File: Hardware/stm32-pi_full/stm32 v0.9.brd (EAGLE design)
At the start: 131.4 x 105.8 mm, 272 parts, among them J1 SOLDERJUMPERNO, Q1 MMBT3906, Q2 MMBT3904, Q3 MMBT3904, U1 ESP32-WROOM-32D, Y1 6MM_3.5MM_CRYSTAL

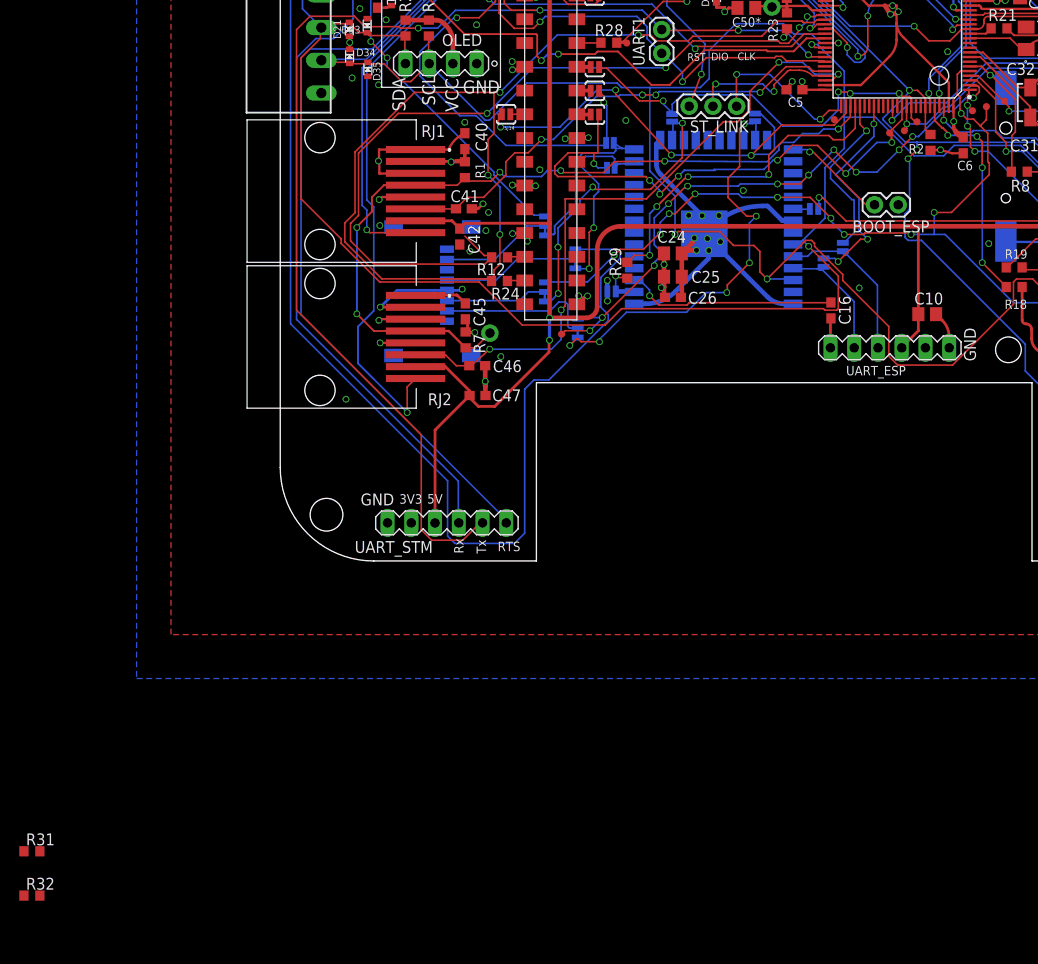
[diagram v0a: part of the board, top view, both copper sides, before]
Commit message: non-Blocking UART transmissions
Saving 40ms at 460800 baud or 160ms at 115200 baud.
Now takes less than a millisecond to begin the UART transmit, happens in the background.
notes included on how to fire UART transmissions consequtively withing messing up the buffer or dropping transmissions.
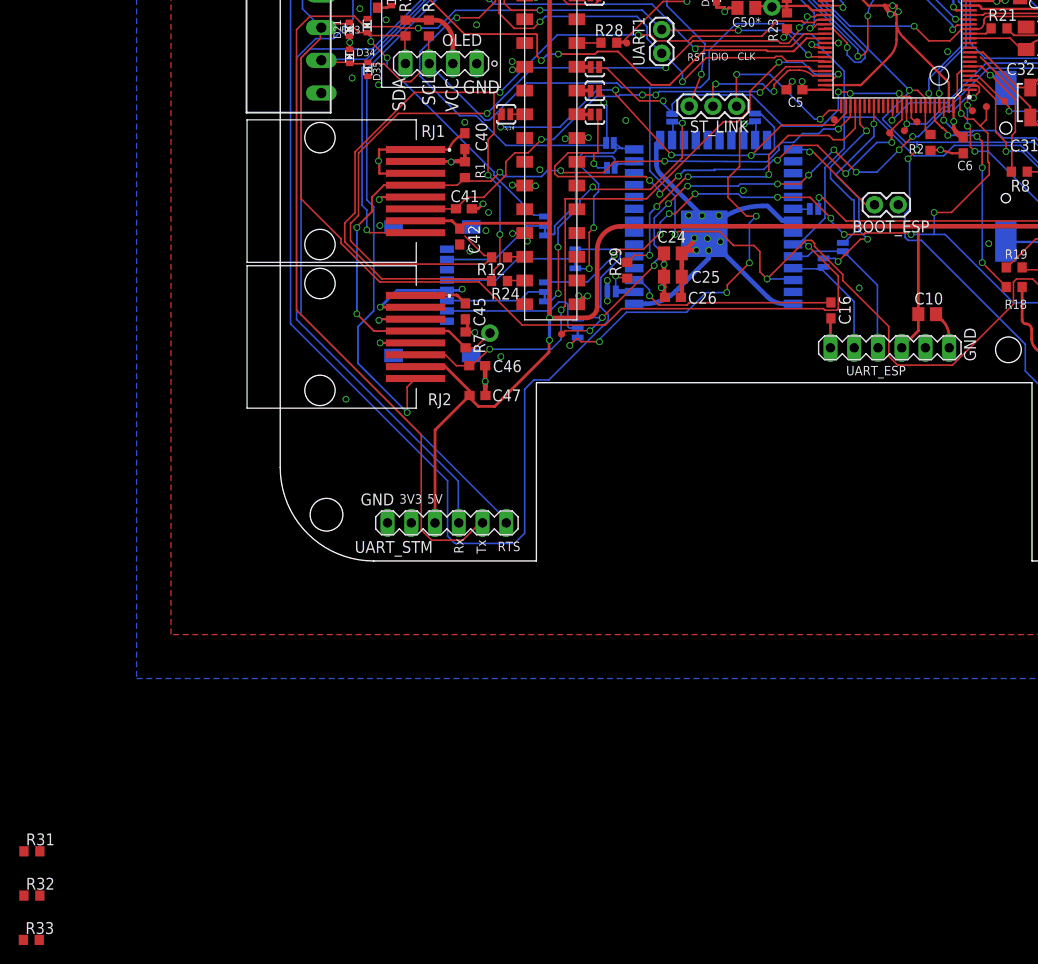
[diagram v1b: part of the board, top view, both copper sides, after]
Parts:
- added R33: 0R, rcl:R0603
- C29, C30: value 4.7nF -> 15pF
- C31, C32: value 2.2uF -> 10pF
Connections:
- new net N$1: R33.2, STM32F303VE.8
- net PC14: now also R33.1; no longer STM32F303VE.8
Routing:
- net PC14: track 12.9 -> 11.7 mm
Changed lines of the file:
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@@
 <attribute name="VALUE" x="120.97" y="40.14" size="1.27" layer="27" rot="R180"/>
 </element>
-<element name="C29" library="rcl" library_urn="urn:adsk.eagle:library:334" package="C0603" package3d_urn="urn:adsk.eagle:package:23616/2" value="4.7nF" x="87.0936875" y="57.0890375" smashed="yes">
+<element name="C29" library="rcl" library_urn="urn:adsk.eagle:library:334" package="C0603" package3d_urn="urn:adsk.eagle:package:23616/2" value="15pF" x="87.0936875" y="57.0890375" smashed="yes">
 <attribute name="NAME" x="88.71165625" y="58.977115625" size="1.27" layer="25" rot="R270"/>
 <attribute name="POPULARITY" value="73" x="87.0936875" y="57.0890375" size="1.778" layer="27" display="off"/>
@@
 <attribute name="VALUE" x="86.4586875" y="55.1840375" size="1.27" layer="27"/>
 </element>
-<element name="C30" library="rcl" library_urn="urn:adsk.eagle:library:334" package="C0603" package3d_urn="urn:adsk.eagle:package:23616/2" value="4.7nF" x="87.10355" y="54.8606875" smashed="yes">
+<element name="C30" library="rcl" library_urn="urn:adsk.eagle:library:334" package="C0603" package3d_urn="urn:adsk.eagle:package:23616/2" value="15pF" x="87.10355" y="54.8606875" smashed="yes">
 <attribute name="NAME" x="85.607396875" y="52.7083" size="1.27" layer="25"/>
 <attribute name="POPULARITY" value="73" x="87.10355" y="54.8606875" size="1.778" layer="27" display="off"/>
@@
 <attribute name="VALUE" x="86.46855" y="52.9556875" size="1.27" layer="27"/>
 </element>
-<element name="C31" library="rcl" library_urn="urn:adsk.eagle:library:334" package="C0805" package3d_urn="urn:adsk.eagle:package:23617/2" value="2.2uF" x="83.002" y="45.078" smashed="yes">
+<element name="C31" library="rcl" library_urn="urn:adsk.eagle:library:334" package="C0805" package3d_urn="urn:adsk.eagle:package:23617/2" value="10pF" x="83.002" y="45.078" smashed="yes">
 <attribute name="NAME" x="78.045440625" y="43.81645" size="1.27" layer="25"/>
 <attribute name="POPULARITY" value="88" x="83.002" y="45.078" size="1.778" layer="27" display="off"/>
@@
 <attribute name="VALUE" x="81.732" y="42.538" size="1.27" layer="27"/>
 </element>
-<element name="C32" library="rcl" library_urn="urn:adsk.eagle:library:334" package="C0805" package3d_urn="urn:adsk.eagle:package:23617/2" value="2.2uF" x="83" y="52.5" smashed="yes">
+<element name="C32" library="rcl" library_urn="urn:adsk.eagle:library:334" package="C0805" package3d_urn="urn:adsk.eagle:package:23617/2" value="10pF" x="83" y="52.5" smashed="yes">
 <attribute name="NAME" x="77.667828125" y="51.983675" size="1.27" layer="25"/>
 <attribute name="POPULARITY" value="88" x="83" y="52.5" size="1.778" layer="27" display="off"/>
@@
 <attribute name="VALUE" x="-27.197559375" y="-37.693090625" size="1.27" layer="27"/>
 </element>
+<element name="R33" library="rcl" library_urn="urn:adsk.eagle:library:334" package="R0603" package3d_urn="urn:adsk.eagle:package:23555/3" value="0R" x="-26.62351875" y="-40.529509375" smashed="yes">
+<attribute name="NAME" x="-27.25851875" y="-39.894509375" size="1.27" layer="25"/>
+<attribute name="POPULARITY" value="70" x="-26.62351875" y="-40.529509375" size="1.778" layer="27" display="off"/>
+<attribute name="SPICEPREFIX" value="R" x="-26.62351875" y="-40.529509375" size="1.778" layer="27" display="off"/>
+<attribute name="VALUE" x="-27.25851875" y="-42.434509375" size="1.27" layer="27"/>
+</element>
 </elements>
 <signals>
@@
 </signal>
 <signal name="PC14">
-<contactref element="STM32F303VE" pad="8"/>
 <contactref element="LSE" pad="P$1"/>
-<wire x1="73.75" y1="53.9" x2="74.9036375" y2="53.9" width="0.2032" layer="1"/>
 <wire x1="80.226" y1="48.5776375" x2="80.226" y2="47.438" width="0.2032" layer="1"/>
 <wire x1="74.9036375" y1="53.9" x2="80.226" y2="48.5776375" width="0.2032" layer="1"/>
@@
 <wire x1="80.226" y1="47.438" x2="81.67440625" y2="45.98959375" width="0.254" layer="1"/>
 <wire x1="81.67440625" y1="45.98959375" x2="82.052" y2="45.078" width="0.254" layer="1" curve="-45"/>
+<contactref element="R33" pad="1"/>
+<wire x1="-27.47351875" y1="-40.529509375" x2="82.052" y2="45.078" width="0" layer="19" extent="1-1"/>
 </signal>
 <signal name="PC15">
@@
 <via x="35.8775" y="30.48" extent="1-16" drill="0.5"/>
 </signal>
+<signal name="N$1">
+<contactref element="STM32F303VE" pad="8"/>
+<contactref element="R33" pad="2"/>
+<wire x1="-25.77351875" y1="-40.529509375" x2="73.75" y2="53.9" width="0" layer="19" extent="1-1"/>
+</signal>
 </signals>

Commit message: minor, uipdate BoMs
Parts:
- R21: value 0R -> 2k
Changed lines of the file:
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@@
 <attribute name="VALUE" x="11.495" y="57.635" size="1.27" layer="27" rot="R270"/>
 </element>
-<element name="R21" library="resistor" package="R0603" value="0R" x="76.883209375" y="56.964225" smashed="yes">
+<element name="R21" library="resistor" package="R0603" value="2k" x="76.883209375" y="56.964225" smashed="yes">
 <attribute name="NAME" x="78.810725" y="59.036134375" size="1.27" layer="25" rot="R180"/>
 <attribute name="VALUE" x="76.248209375" y="55.059225" size="1.27" layer="27"/>

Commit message: minor changes, some checks on proto v0.8 done.
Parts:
- removed Q4: (no value), microbuilder:SOT23-R
- added C20, C34: 100nF, rcl:C0603
- added D36, D37: ESD5Z3.3T1G, microbuilder:SOD-523
- R34, R35, R36: value (none) -> 0R
- R8: value 1.5k -> 100k
- renumbered JP4 to R34, JP5 to R35, JP6 to R36
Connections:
- new net N$19: D37.K, R8.1
- net +3V3: no longer Q4.3
- net +5V: now also D36.A
- net GND: now also C20.2; no longer Q4.1
- net N$16: now also D36.K, D37.A; no longer Q4.2, R8.1
- net NRST_STM: now also C34.1, C34.2
- net VBAT: now also C20.1
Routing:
- net N$16: track 1.93 -> 0.00 mm
- net BIAS: track 588.4 -> 587.1 mm
- net GND: track 296.9 -> 295.6 mm, vias 143 -> 142
- net +3V3: track 143.8 -> 143.0 mm, vias 41 -> 40

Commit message: Various checks.
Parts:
- added C35, C36: 2.2uF, rcl:C0805
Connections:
- net BIAS: now also C35.1, C36.1
- net GND: now also C35.2, C36.2
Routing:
- net RST_RFM: track 86.5 -> 87.3 mm

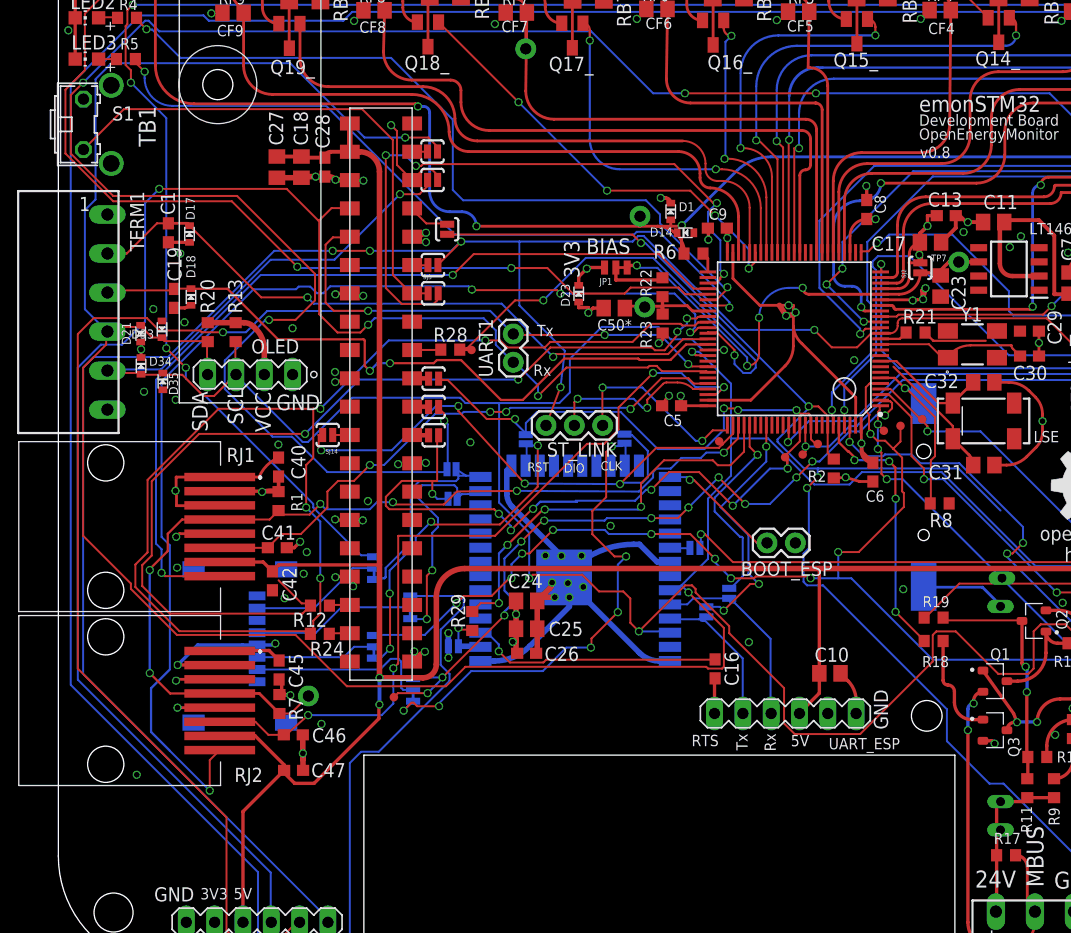
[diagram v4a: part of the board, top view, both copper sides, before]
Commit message: backup various changes
JSON parser tidy
RESET CAUSE reported, and reset counter in RTC backup RAM.
RFM69 Implementation improvements: removed annecessary SPI transactions while waiting for a Rx.
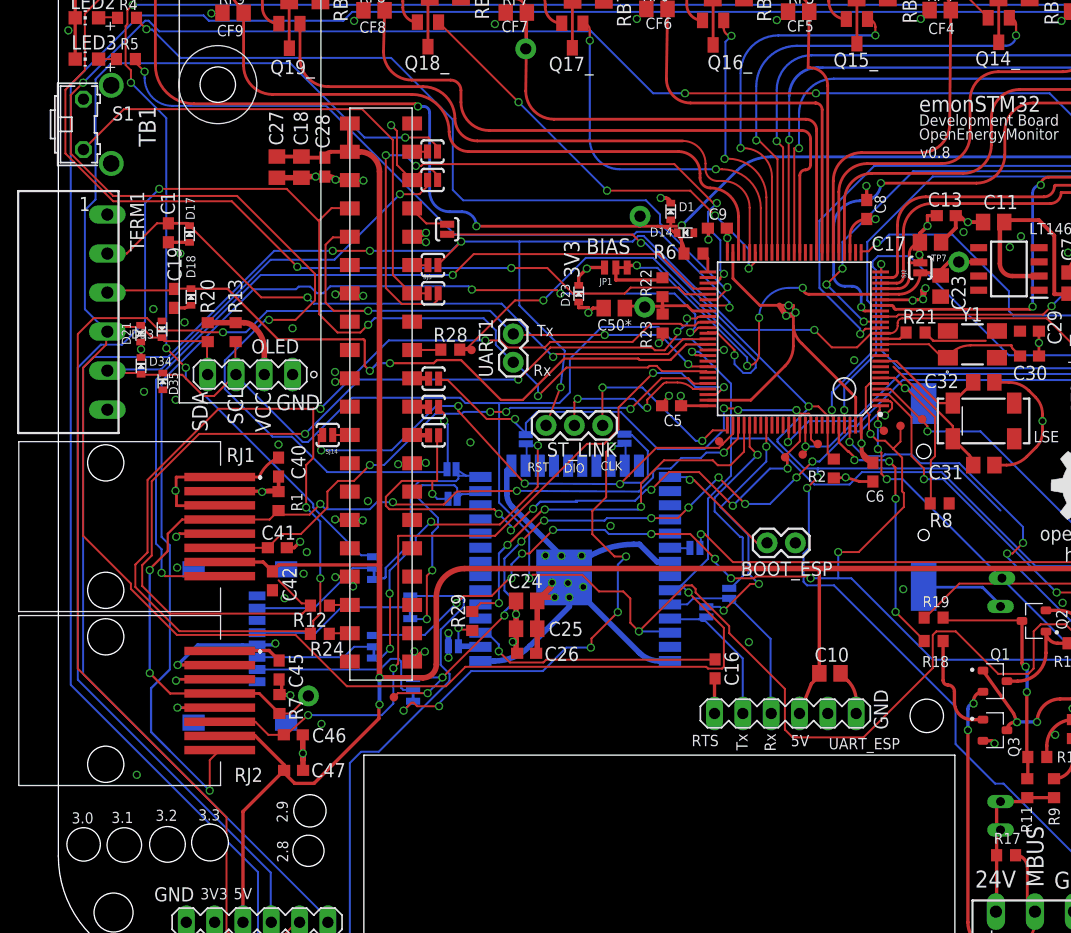
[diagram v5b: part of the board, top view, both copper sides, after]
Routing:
- net SCL: track 224.5 -> 225.3 mm
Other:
- board text added: "2.8"
- board text added: "2.9"
- board text added: "3.0"
- board text added: "3.1"
- board text added: "3.2"
- board text added: "3.3"
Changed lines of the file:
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@@
 <setting verticaltext="up"/>
 </settings>
-<grid distance="0.01" unitdist="mil" unit="mil" style="lines" multiple="1" display="no" altdistance="5" altunitdist="mil" altunit="mil"/>
+<grid distance="0.01" unitdist="mil" unit="mm" style="lines" multiple="1" display="no" altdistance="5" altunitdist="mil" altunit="mil"/>
 <layers>
 <layer number="1" name="Top" color="4" fill="1" visible="yes" active="yes"/>
@@
 <layer number="43" name="vRestrict" color="2" fill="10" visible="no" active="yes"/>
 <layer number="44" name="Drills" color="7" fill="1" visible="no" active="yes"/>
-<layer number="45" name="Holes" color="7" fill="1" visible="no" active="yes"/>
+<layer number="45" name="Holes" color="7" fill="1" visible="yes" active="yes"/>
 <layer number="46" name="Milling" color="3" fill="1" visible="no" active="yes"/>
 <layer number="47" name="Measures" color="7" fill="1" visible="no" active="yes"/>
@@
 <text x="95.377" y="58.928" size="1.016" layer="25" rot="R270" align="bottom-center">5V</text>
 <text x="95.377" y="61.468" size="1.016" layer="25" rot="R270" align="bottom-center">3V3</text>
-<hole x="14.3" y="79.2" drill="2.7"/>
+<hole x="14.3" y="79.2" drill="3.18"/>
 <circle x="14.3" y="79.2" radius="3.5" width="0.1" layer="21"/>
 <text x="19.52678125" y="50.00084375" size="1.4" layer="25">GND</text>
@@
 <text x="44.21149375" y="54.102759375" size="1.016" layer="25" rot="R180">Rx</text>
 <text x="44.4332375" y="57.6572375" size="1.016" layer="25" rot="R180">Tx</text>
+<hole x="2.26695" y="11.05966875" drill="3"/>
+<hole x="5.916421875" y="11.004296875" drill="3.1"/>
+<hole x="9.786875" y="11.05966875" drill="3.2"/>
+<hole x="13.601953125" y="11.22553125" drill="3.3"/>
+<hole x="22.561803125" y="14.06880625" drill="2.9"/>
+<hole x="22.4289625" y="10.48511875" drill="2.8"/>
+<text x="1.189990625" y="12.93698125" size="1" layer="21">3.0</text>
+<text x="4.7602125" y="12.975590625" size="1" layer="21">3.1</text>
+<text x="8.7144875" y="13.167359375" size="1" layer="21">3.2</text>
+<text x="12.553440625" y="13.2057125" size="1" layer="21">3.3</text>
+<text x="20.57679375" y="13.01394375" size="1" layer="21" rot="R90">2.9</text>
+<text x="20.615403125" y="9.44371875" size="1" layer="21" rot="R90">2.8</text>
 </plain>
 <attributes>
@@
 <wire x1="101.908896875" y1="35.8" x2="103.70495" y2="36.54395" width="0.5" layer="1" curve="45"/>
 <wire x1="103.70495" y1="36.54395" x2="104.721" y2="37.56" width="0.5" layer="1"/>
-<wire x1="68.25" y1="24.625" x2="68.25" y2="26.4" width="0.3048" layer="1"/>
-<wire x1="66.5" y1="22.875" x2="68.25" y2="24.625" width="0.3048" layer="1"/>
-<wire x1="66.5" y1="22.875" x2="66.47" y2="22.8" width="0.3048" layer="1"/>
+<wire x1="68.25" y1="26.17973125" x2="68.25" y2="26.4" width="0.3048" layer="1"/>
+<wire x1="67.5364875" y1="25.46621875" x2="68.25" y2="26.17973125" width="0.3048" layer="1"/>
+<wire x1="67.5364875" y1="25.46621875" x2="66.47" y2="22.8" width="0.3048" layer="1"/>
 <wire x1="68.25" y1="35.8" x2="68.25" y2="26.4" width="0.3048" layer="1"/>
 <wire x1="19.75" y1="36.125" x2="28.8" y2="36.125" width="0.3048" layer="1"/>
@@
 <wire x1="92.23375" y1="9.04875" x2="92.23375" y2="4.92125" width="0.1778" layer="16"/>
 <wire x1="84.7725" y1="16.51" x2="92.23375" y2="9.04875" width="0.1778" layer="16"/>
-<wire x1="83.5025" y1="16.51" x2="84.7725" y2="16.51" width="0.1778" layer="16"/>
-<wire x1="79.6925" y1="20.32" x2="83.5025" y2="16.51" width="0.1778" layer="16"/>
-<wire x1="79.6925" y1="23.1775" x2="79.6925" y2="20.32" width="0.1778" layer="16"/>
-<wire x1="68.58" y1="34.29" x2="79.6925" y2="23.1775" width="0.1778" layer="16"/>
-<wire x1="67.15125" y1="34.29" x2="68.58" y2="34.29" width="0.1778" layer="16"/>
+<wire x1="84.0143125" y1="16.51" x2="84.7725" y2="16.51" width="0.1778" layer="16"/>
+<wire x1="80.46745625" y1="20.05685625" x2="84.0143125" y2="16.51" width="0.1778" layer="16"/>
+<wire x1="80.46745625" y1="23.397209375" x2="80.46745625" y2="20.05685625" width="0.1778" layer="16"/>
+<wire x1="69.574665625" y1="34.29" x2="80.46745625" y2="23.397209375" width="0.1778" layer="16"/>
+<wire x1="67.15125" y1="34.29" x2="69.574665625" y2="34.29" width="0.1778" layer="16"/>
 <wire x1="66.83375" y1="34.6075" x2="67.15125" y2="34.29" width="0.1778" layer="16"/>
 <wire x1="66.83375" y1="37.1475" x2="66.83375" y2="34.6075" width="0.1778" layer="16"/>
@@
 <wire x1="78.74" y1="30.1625" x2="80.48625" y2="30.1625" width="0.1778" layer="1"/>
 <wire x1="78.4225" y1="29.845" x2="78.74" y2="30.1625" width="0.1778" layer="1"/>
-<wire x1="78.4225" y1="27.46375" x2="78.4225" y2="29.845" width="0.1778" layer="1"/>
-<wire x1="71.91375" y1="20.955" x2="78.4225" y2="27.46375" width="0.1778" layer="1"/>
-<wire x1="66.04" y1="20.955" x2="71.91375" y2="20.955" width="0.1778" layer="1"/>
-<wire x1="65.0875" y1="21.9075" x2="66.04" y2="20.955" width="0.1778" layer="1"/>
-<wire x1="65.0875" y1="25.0825" x2="65.0875" y2="21.9075" width="0.1778" layer="1"/>
-<wire x1="60.16625" y1="30.00375" x2="65.0875" y2="25.0825" width="0.1778" layer="1"/>
+<wire x1="78.4225" y1="26.871421875" x2="78.4225" y2="29.845" width="0.1778" layer="1"/>
+<wire x1="72.2099125" y1="20.658834375" x2="78.4225" y2="26.871421875" width="0.1778" layer="1"/>
+<wire x1="65.85483125" y1="20.658834375" x2="72.2099125" y2="20.658834375" width="0.1778" layer="1"/>
+<wire x1="65.1614125" y1="21.352253125" x2="65.85483125" y2="20.658834375" width="0.1778" layer="1"/>
+<wire x1="65.1614125" y1="25.0085875" x2="65.1614125" y2="21.352253125" width="0.1778" layer="1"/>
+<wire x1="60.16625" y1="30.00375" x2="65.1614125" y2="25.0085875" width="0.1778" layer="1"/>
 <wire x1="60.16625" y1="30.63875" x2="60.16625" y2="30.00375" width="0.1778" layer="1"/>
 <wire x1="57.15" y1="33.655" x2="60.16625" y2="30.63875" width="0.1778" layer="1"/>
